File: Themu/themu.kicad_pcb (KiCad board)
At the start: 2 copper layers, 47 parts, among them J1 USB_B_Micro, J2 Conn_01x02, J3 Conn_01x08, Q1 mmbt2222, Q2 mmbt2222, Q3 DMP2045U, U1 CP2104, U2 AP2112K-3.3, U3 ESP32-WROOM-32, U4 MCP73831-2-OT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

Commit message: Routed completed
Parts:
- removed D1: RED LED, LED_SMD:LED_0603_1608Metric_Pad1.05x0.95mm_HandSolder
- added L1: RGB LED, LED APTF1616LSEEZGKQBKC:LED APTF1616LSEEZGKQBKC, F.Cu at (111.5, 76.1)
- added R20: 1K, Resistor_SMD:R_0603_1608Metric_Pad1.05x0.95mm_HandSolder, B.Cu at (111.1, 65.9)
- added R21: 1K, Resistor_SMD:R_0603_1608Metric_Pad1.05x0.95mm_HandSolder, B.Cu at (109.6, 65.9)
- C10, C11, C12, C13, C9, J3, R11, R12, R13, R14, R15, R16, R17, R18, R19, R3, R5, U5: moved to B.Cu
- moved J3 72.9 mm to (94.5, 87.1)
- moved C11 62.1 mm to (108.5, 54.7), turned to 90 degrees
- moved U5 60.0 mm to (106.4, 60.2)
- moved R13 58.9 mm to (105.4, 54.7), turned to 90 degrees
- moved R17 57.7 mm to (103.9, 48.4), turned to 270 degrees
- moved R12 56.9 mm to (106.6, 65.9), turned to 90 degrees
- moved C10 56.0 mm to (106.9, 54.7), turned to 90 degrees
- moved R18 56.0 mm to (102.4, 48.4), turned to 270 degrees
- moved R15 54.1 mm to (106.9, 48.4), turned to 270 degrees
- moved C12 52.8 mm to (110.0, 54.7), turned to 90 degrees
- moved R14 50.7 mm to (105.0, 65.9), turned to 90 degrees
- moved R16 48.2 mm to (105.4, 48.4), turned to 270 degrees
- moved R19 47.9 mm to (100.8, 48.4), turned to 270 degrees
- moved C9 46.4 mm to (99.3, 48.4), turned to 90 degrees
- moved C13 45.2 mm to (103.5, 65.9), turned to 270 degrees
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- renumbered D3 to L2
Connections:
- J1 pad 4: Net-(J1-Pad4) -> (no net)
- J3 pad 1: +3V3 -> GND
- J3 pad 8: GND -> +3V3
- R3 pad 1: +3V3 -> /ESP32-WROOM-32/IO12
- U1 pad 1: Net-(U1-Pad1) -> (no net)
- U1 pad 10: Net-(U1-Pad10) -> (no net)
- U1 pad 11: Net-(U1-Pad11) -> (no net)
- U1 pad 12: Net-(U1-Pad12) -> (no net)
- U1 pad 13: Net-(U1-Pad13) -> (no net)
- U1 pad 14: Net-(U1-Pad14) -> (no net)
- U1 pad 15: Net-(U1-Pad15) -> (no net)
- U1 pad 16: Net-(U1-Pad16) -> (no net)
- U1 pad 17: Net-(U1-Pad17) -> (no net)
- U1 pad 18: Net-(U1-Pad18) -> (no net)
- U1 pad 22: Net-(U1-Pad22) -> (no net)
- U1 pad 24: Net-(U1-Pad24) -> (no net)
- U1 pad 9: Net-(U1-Pad9) -> (no net)
- U2 pad 4: Net-(U2-Pad4) -> (no net)
- U3 pad 10: Net-(U3-Pad10) -> /ESP32-WROOM-32/BTN
- U3 pad 11: Net-(U3-Pad11) -> /ESP32-WROOM-32/IO26
- U3 pad 12: Net-(U3-Pad12) -> /ESP32-WROOM-32/IO27
- U3 pad 13: Net-(U3-Pad13) -> (no net)
- U3 pad 14: /ESP32-WROOM-32/BTN -> /ESP32-WROOM-32/IO12
- U3 pad 16: /ESP32-WROOM-32/IO13 -> (no net)
- U3 pad 17: Net-(U3-Pad17) -> (no net)
- U3 pad 18: Net-(U3-Pad18) -> (no net)
- U3 pad 19: Net-(U3-Pad19) -> (no net)
- U3 pad 20: Net-(U3-Pad20) -> (no net)
- U3 pad 23: Net-(U3-Pad23) -> (no net)
- U3 pad 24: Net-(U3-Pad24) -> (no net)
- U3 pad 26: Net-(U3-Pad26) -> (no net)
- U3 pad 27: Net-(U3-Pad27) -> (no net)
- U3 pad 28: Net-(U3-Pad28) -> (no net)
- U3 pad 29: Net-(U3-Pad29) -> (no net)
- U3 pad 30: Net-(U3-Pad30) -> (no net)
- U3 pad 31: Net-(U3-Pad31) -> (no net)
- U3 pad 32: Net-(U3-Pad32) -> (no net)
- U3 pad 33: Net-(U3-Pad33) -> (no net)
- U3 pad 36: Net-(U3-Pad36) -> (no net)
- U3 pad 37: Net-(U3-Pad37) -> (no net)
- U3 pad 6: /ESP32-WROOM-32/FLX4 -> /ESP32-WROOM-32/FLX2
- U3 pad 7: /ESP32-WROOM-32/FLX5 -> /ESP32-WROOM-32/FLX3
- U3 pad 8: /ESP32-WROOM-32/FLX2 -> /ESP32-WROOM-32/FLX4
- U3 pad 9: /ESP32-WROOM-32/FLX3 -> /ESP32-WROOM-32/FLX5
- U5 pad 12: /Peripherials/INT -> (no net)
- U5 pad 6: /Peripherials/XDA -> (no net)
- U5 pad 7: /Peripherials/XCL -> (no net)
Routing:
- net GND: track 20.9 -> 251.1 mm, vias 6 -> 16
- net +3V3: track 31.1 -> 121.5 mm, vias 0 -> 6
- net /ESP32-WROOM-32/ADC1_CH0: track 3.33 -> 56.6 mm, vias 0 -> 2
- net /ESP32-WROOM-32/FLX1: track 0.00 -> 53.1 mm, vias 0 -> 1
- net /ESP32-WROOM-32/FLX2: track 0.00 -> 48.5 mm, vias 0 -> 1
- net /ESP32-WROOM-32/FLX3: track 0.00 -> 43.9 mm, vias 0 -> 1
- net /ESP32-WROOM-32/TXD0: track 0.00 -> 42.0 mm, vias 0 -> 2
- net /ESP32-WROOM-32/RXD0: track 0.00 -> 39.6 mm, vias 0 -> 2
- net /ESP32-WROOM-32/FLX4: track 0.00 -> 39.1 mm, vias 0 -> 1
- net /ESP32-WROOM-32/FLX5: track 0.00 -> 35.6 mm, vias 0 -> 1
- net /ESP32-WROOM-32/BTN: track 0.00 -> 29.9 mm, vias 0 -> 1
- net VBUS: track 55.8 -> 29.2 mm, vias 2 -> 0
- net +BATT: track 40.2 -> 14.2 mm
- net /ESP32-WROOM-32/EN: track 9.93 -> 35.0 mm, vias 1 -> 3
- net /ESP32-WROOM-32/IO26: track 0.00 -> 19.6 mm, vias 0 -> 1
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
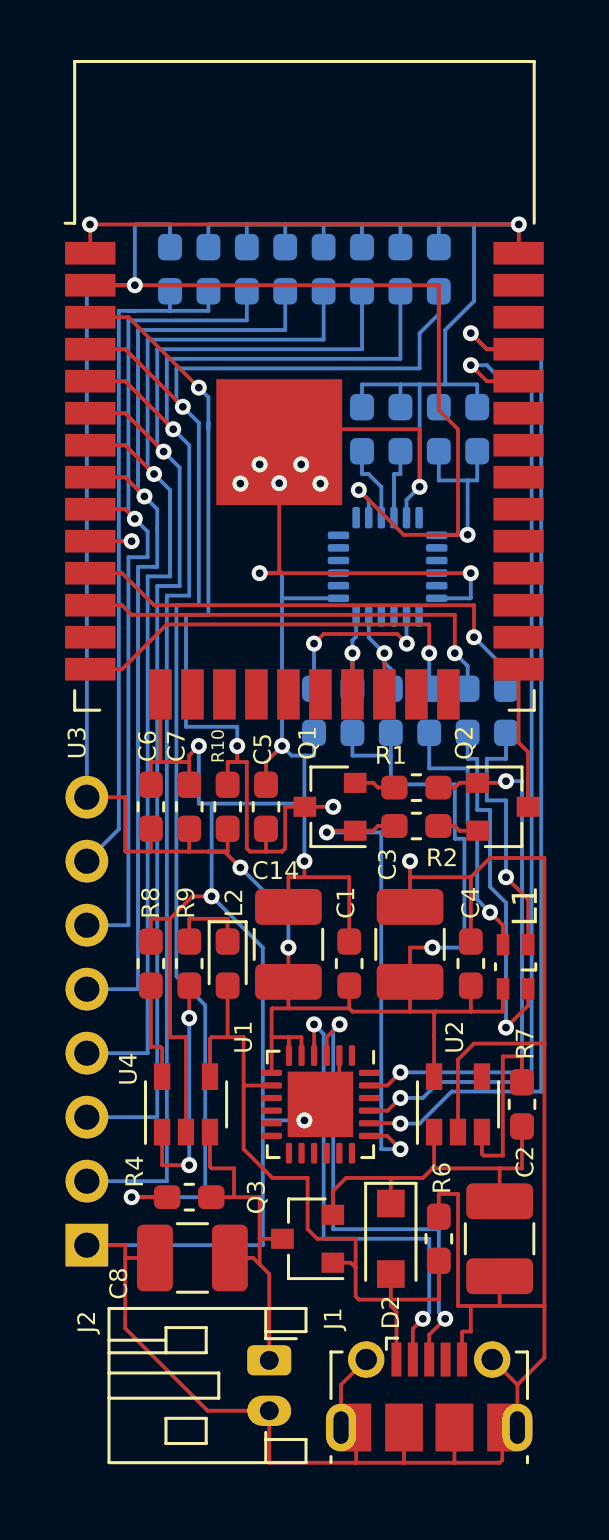
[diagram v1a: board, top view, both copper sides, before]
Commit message: RGB Led (L1) footprint updated
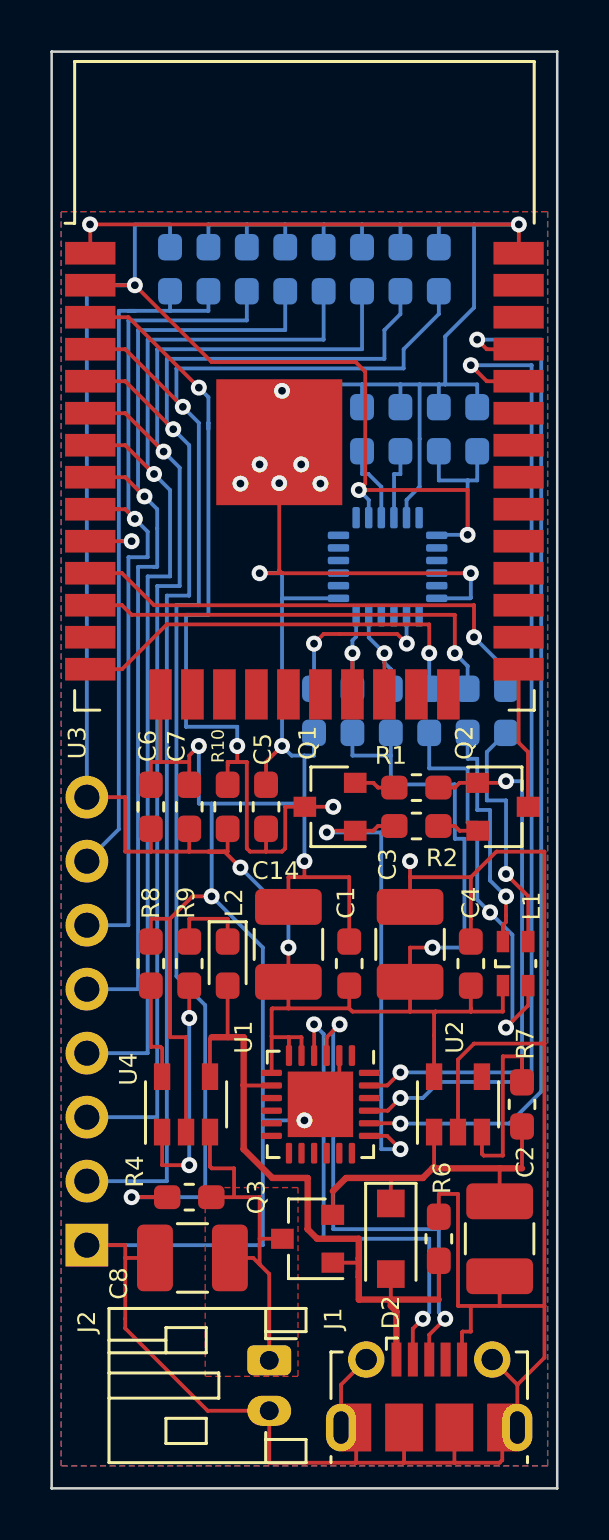
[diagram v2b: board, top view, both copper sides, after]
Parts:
- L1: value RGB LED -> LED_ARGB; footprint LED APTF1616LSEEZGKQBKC:LED APTF1616LSEEZGKQBKC -> Themu_FP_Lib:LED APTF1616LSEEZGKQBKC
- moved L1 0.13 mm to (111.5, 75.9)
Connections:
- L1 pad 1: Net-(L1-Pad1) -> +3V3
- L1 pad 4: +3V3 -> Net-(L1-Pad4)
- R20 pad 2: Net-(L1-Pad2) -> Net-(L1-Pad3)
- R21 pad 2: Net-(L1-Pad1) -> Net-(L1-Pad2)
- R3 pad 2: Net-(L1-Pad3) -> Net-(L1-Pad4)
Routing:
- net Net-(L1-Pad4): track 0.00 -> 16.2 mm, vias 0 -> 2
- net Net-(L1-Pad1): track 14.8 -> 0.00 mm, vias 1 -> 0
- net +3V3: track 121.5 -> 115.6 mm
- net GND: track 251.1 -> 247.4 mm
- net Net-(L1-Pad3): track 10.7 -> 9.85 mm
- net Net-(L1-Pad2): track 10.3 -> 9.48 mm
- net VBUS: track 29.2 -> 29.9 mm
- added copper zone on F.Cu, net +BATT
- added copper zone on B.Cu, net GND
- added copper zone on F.Cu, net GND
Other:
- board outline added: 20.1 x 57 mm
